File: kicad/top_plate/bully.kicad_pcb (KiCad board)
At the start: 2 copper layers, 256.3 x 75.4 mm, 50 parts, among them SW1 SW_Push, SW10 SW_Push, SW11 SW_Push, SW12 SW_Push, SW13 SW_Push, SW14 SW_Push, SW15 SW_Push, SW16 SW_Push, SW17 SW_Push, SW18 SW_Push, SW19 SW_Push, SW2 SW_Push, SW20 SW_Push, SW21 SW_Push, SW22 SW_Push, SW23 SW_Push, SW24 SW_Push, SW25 SW_Push, SW26 SW_Push, SW27 SW_Push, SW28 SW_Push, SW29 SW_Push, SW3 SW_Push, SW30 SW_Push, SW31 SW_Push, SW32 SW_Push, SW33 SW_Push, SW34 SW_Push, SW35 SW_Push, SW36 SW_Push, SW37 SW_Push, SW38 SW_Push, SW39 SW_Push, SW4 SW_Push, SW40 SW_Push, SW41 SW_Push, SW42 SW_Push, SW43 SW_Push, SW44 SW_Push, SW45 SW_Push, SW46 SW_Push, SW47 SW_Push, SW48 SW_Push, SW49 SW_Push, SW5 SW_Push, SW50 SW_Push, SW6 SW_Push, SW7 SW_Push, SW8 SW_Push, SW9 SW_Push

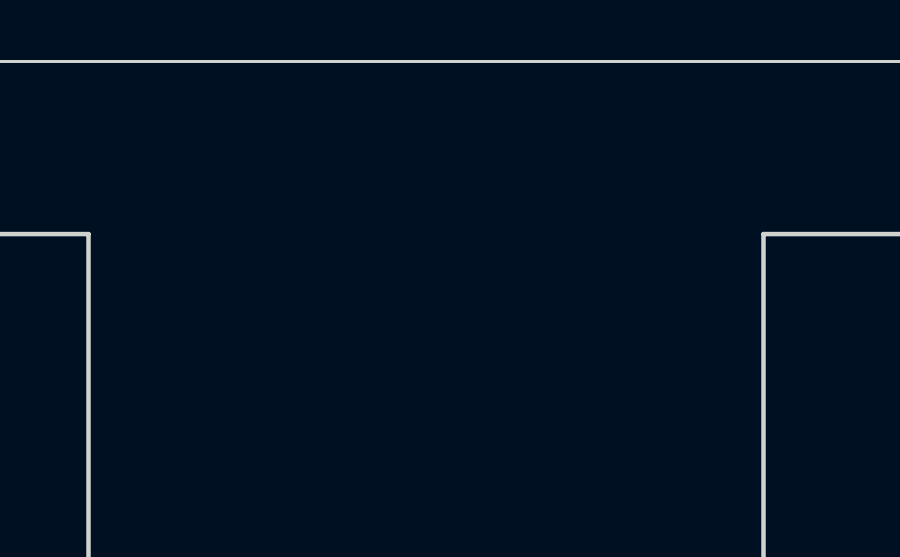
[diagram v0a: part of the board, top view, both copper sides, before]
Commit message: Modified top plate model.
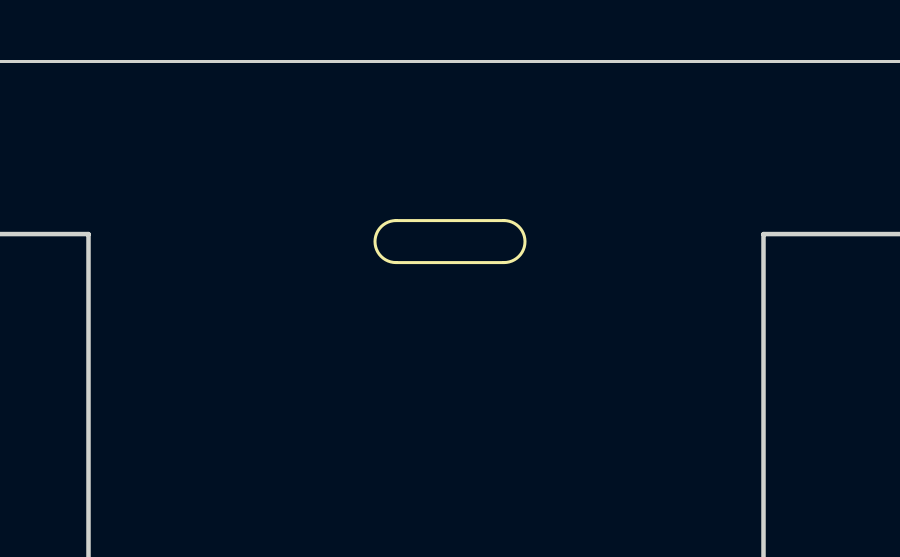
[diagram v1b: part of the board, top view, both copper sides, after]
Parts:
- added **: Hole_R, colbully:TopPlate_LedHole2, F.Cu at (142.0, 60.0)
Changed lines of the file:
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@@
+		)
+	)
+	(footprint "colbully:TopPlate_LedHole2"
+		(layer "F.Cu")
+		(at 142 60)
+		(descr "Resitance 3 pas")
+		(tags "R")
+		(property "Reference" "**"
+			(at 0.05 -0.08 0)
+			(layer "F.SilkS")
+			(hide yes)
+			(effects
+				(font
+					(size 0.8128 0.8128)
+					(thickness 0.15)
+				)
+			)
+		)
+		(property "Value" "Hole_R"
+			(at 0 -1.6 0)
+			(layer "F.SilkS")
+			(hide yes)
+			(effects
+				(font
+					(size 0.5 0.5)
+					(thickness 0.125)
+				)
+			)
+		)
+		(property "Footprint" "colbully:TopPlate_LedHole2"
+			(at 0.07 1.66 0)
+			(unlocked yes)
+			(layer "F.Fab")
+			(hide yes)
+			(effects
+				(font
+					(size 1.27 1.27)
+				)
+			)
+		)
+		(property "Datasheet" ""
+			(at 0 0 0)
+			(unlocked yes)
+			(layer "F.Fab")
+			(hide yes)
+			(effects
+				(font
+					(size 1.27 1.27)
+				)
+			)
+		)
+		(property "Description" ""
+			(at 0 0 0)
+			(unlocked yes)
+			(layer "F.Fab")
+			(hide yes)
+			(effects
+				(font
+					(size 1.27 1.27)
+				)
+			)
+		)
+		(attr through_hole)
+		(fp_line
+			(start -1.8 -0.7)
+			(end 1.8 -0.7)
+			(stroke
+				(width 0.1)
+				(type default)
+			)
+			(layer "F.SilkS")
+		)
+		(fp_line
+			(start -1.8 0.7)
+			(end 1.8 0.7)
+			(stroke
+				(width 0.1)
+				(type default)
+			)
+			(layer "F.SilkS")
+		)
+		(fp_arc
+			(start -1.8 0.7)
+			(mid -2.5 0)
+			(end -1.8 -0.7)
+			(stroke
+				(width 0.1)
+				(type default)
+			)
+			(layer "F.SilkS")
+		)
+		(fp_arc
+			(start 1.8 -0.7)
+			(mid 2.5 0)
+			(end 1.8 0.7)
+			(stroke
+				(width 0.1)
+				(type default)
+			)
+			(layer "F.SilkS")
+		)
+		(model "discret/resistor.wrl"
+			(offset
+				(xyz 0 0 0)
+			)
+			(scale
+				(xyz 0.3 0.3 0.3)
+			)
+			(rotate
+				(xyz 0 0 0)
+			)
+		)
+		(model "Resistors_ThroughHole.3dshapes/Resistor_Horizontal_RM10mm.wrl"
+			(offset
+				(xyz 0 0 0)
+			)
+			(scale
+				(xyz 0.2 0.2 0.2)
+			)
+			(rotate
+				(xyz 0 0 0)
+			)
 		)
 	)
@@
 		)
 	)
-	(gr_circle
-		(center 144.3025 71.47875)
-		(end 144.2025 71.57875)
-		(stroke
-			(width 0.15)
-			(type default)
-		)
-		(fill none)
-		(layer "B.SilkS")
-	)
-	(gr_circle
-		(center 138.50375 83.86875)
-		(end 138.40375 83.96875)
-		(stroke
-			(width 0.15)
-			(type default)
-		)
-		(fill none)
-		(layer "B.SilkS")
-	)
 	(gr_line
